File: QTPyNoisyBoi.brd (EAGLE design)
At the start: 30.5 x 128.5 mm, 32 parts, among them IC1 LD117AS50TR, IC2 TL074D, J1 WQP-PJ301M-12_JACK, J2 WQP-PJ301M-12_JACK, J3 WQP-PJ301M-12_JACK, J4 WQP-PJ301M-12_JACK, U1 ADAFRUIT_QTPYM0

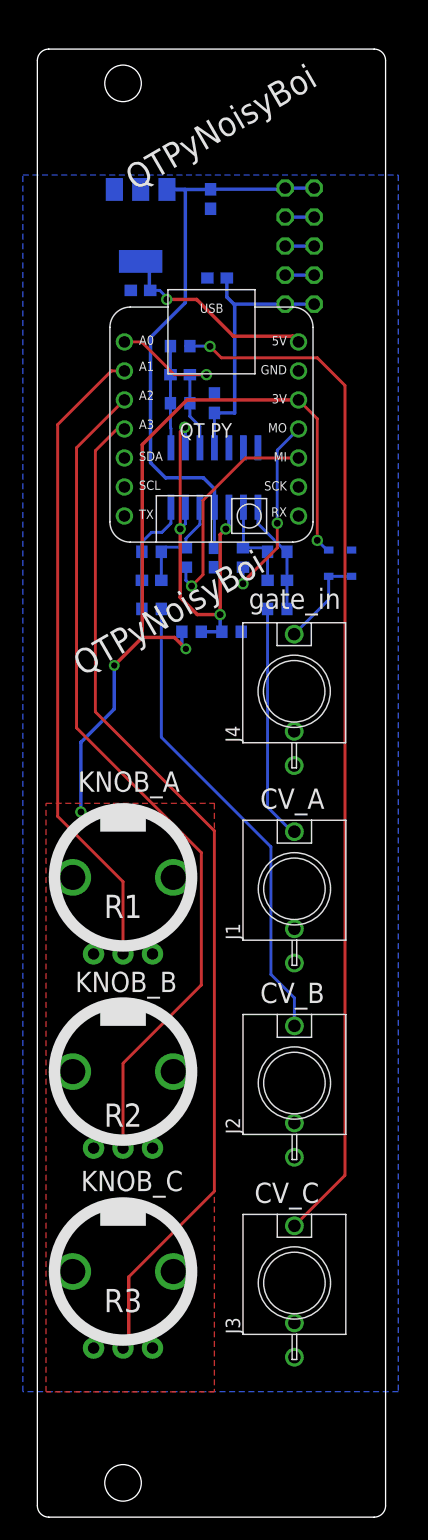
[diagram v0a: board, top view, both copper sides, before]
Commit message: added cap on vmidref; various cleanup
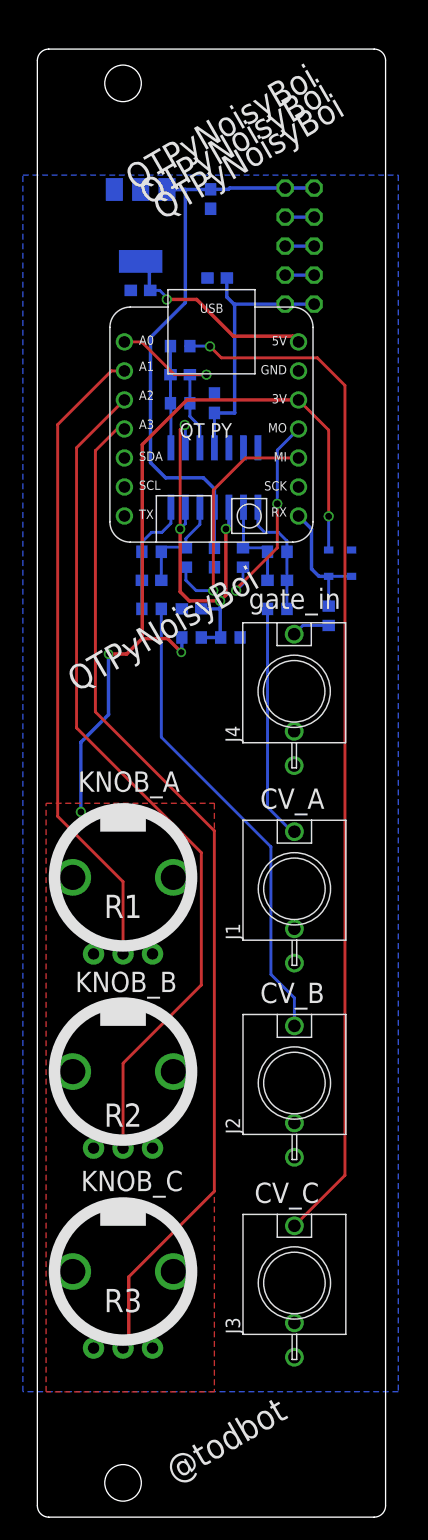
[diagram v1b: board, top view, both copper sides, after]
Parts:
- added C9: (no value), rcl:C0603
- added R14: (no value), rcl:R0603
- moved R11 0.51 mm to (16.9, 77.0)
- moved R10 0.50 mm to (13.5, 77.0)
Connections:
- new net N$5: J4.P$1, R14.2
- net GND: now also C9.1
- net RX: now also R14.1, U1.RX; no longer J4.P$1
- net VMIDREF: now also C9.2
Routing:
- net N$5: track 0.00 -> 3.34 mm
- net RX: track 8.31 -> 11.5 mm
- net N$6: track 17.0 -> 18.7 mm
- net N$7: track 19.7 -> 21.3 mm
- net VMIDREF: track 36.2 -> 37.8 mm
- net N$9: track 10.0 -> 10.7 mm
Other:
- board text added: "20210324"
- board text added: "@todbot"

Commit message: sigh
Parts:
- added C10: 18pF, rcl:C0603
- added C11: (no value), rcl:C0603
- added D3, D4: 250mA/100V, halcyonmod_DiscreteSemi:SOD-323
- added S1: MOMENTARY-SWITCH-SPST-PTH-6.0MM, SparkFun-Switches:TACTILE_SWITCH_PTH_6.0MM
- C4: value (none) -> 0.1uF
- R10, R11: value (none) -> 47k
- R4: value (none) -> 33k
- R5: value (none) -> 100k
- R6: value (none) -> 200
- moved R8 4.00 mm to (10.0, 80.5)
- moved R5 3.91 mm to (20.8, 80.6)
- moved J4 2.99 mm to (20.8, 69.8), turned to 270 degrees
- moved C2 2.55 mm to (16.0, 111.0), turned to 180 degrees
- moved C1 2.05 mm to (16.0, 113.5), turned to 0 degrees
- moved R9 1.30 mm to (10.0, 78.2), turned to 0 degrees
- moved R6 1.02 mm to (20.8, 78.5), turned to 180 degrees
- moved C4 0.73 mm to (20.8, 82.7)
- moved C5 0.60 mm to (10.0, 82.6)
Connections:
- net N$2 renamed A1
- net N$3 renamed A2
- net N$4 renamed A3
- net VMIDREF renamed VBIAS
- removed net N$15: J2.P$1, R9.2
- new net N$12: D4.C, DIM1.1, DIM1.2
- new net N$17: D3.A, DIM1.10, DIM1.9
- new net N$18: C10.2, IC2.1, R6.1
- new net N$2: S1.3, U1.TX
- new net N$8: IC2.13, IC2.14
- net +12V: now also D3.C; no longer DIM1.10, DIM1.9
- net -12V: now also D4.A; no longer DIM1.1, DIM1.2
- net GND: now also IC2.12, S1.1
- net N$1: now also J2.P$1, R9.2; no longer IC2.7, R9.1
- net N$10: now also C10.1
- net N$13: now also C11.1
- net N$14: now also C11.2, IC2.7, R9.1; no longer J1.P$1, R6.2
- net N$9: now also J1.P$1, R6.2; no longer IC2.1, R6.1
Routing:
- net N$15: track 41.3 -> 0.00 mm
- net N$1: track 10.5 -> 45.3 mm, vias 0 -> 1
- net N$18: track 0.00 -> 19.0 mm
- net N$2: track 0.00 -> 16.9 mm
- net A1: track 56.5 -> 72.7 mm
- net N$9: track 10.7 -> 26.4 mm, vias 0 -> 1
- net A3: track 89.5 -> 102.4 mm
- net A2: track 74.6 -> 86.6 mm
- net N$12: track 0.00 -> 7.84 mm
- net +12V: track 51.4 -> 43.9 mm
- net N$17: track 0.00 -> 7.15 mm
- net N$8: track 0.00 -> 5.59 mm
- net +3V3: track 70.1 -> 75.3 mm, vias 4 -> 3
- net N$5: track 3.34 -> 8.35 mm
- net N$10: track 8.36 -> 11.8 mm
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
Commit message: submit to fab
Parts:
- added C12: 18pF, rcl:C0603
- added R144: 220, rcl:R0603
- C1, C2: value (none) -> 1uF
- C11: value (none) -> 18pF
- C3, C5, C6, C7, C8, C9: value (none) -> 0.1uF
- R1, R2, R3: value (none) -> 10k
- R10, R11: value 47k -> 33k
- R12, R7: value (none) -> 33k
- R13, R8: value (none) -> 100k
- R14, R9: value (none) -> 200
- moved R14 28.1 mm to (12.5, 103.8), turned to 0 degrees
- moved R12 2.84 mm to (15.3, 98.0), turned to 270 degrees
- moved C7 2.16 mm to (17.6, 98.0)
- moved R13 0.80 mm to (12.5, 101.7), turned to 0 degrees
- moved C8 0.40 mm to (12.5, 99.6)
- moved C3 0.20 mm to (9.03, 107.6)
- moved R9 0.20 mm to (10.0, 78.4)
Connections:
- removed net N$16: J3.P$1, R13.2
- new net N$3: C12.2, IC2.8, R14.1
- new net N$4: C12.1, C8.1, IC2.10, R12.2, R13.1
- net A0: no longer C8.1, IC2.10
- net N$11: now also J3.P$1, R13.2, R14.2; no longer IC2.8, R12.2, R13.1
- net N$5: now also R144.2; no longer R14.2
- net RX: now also R144.1; no longer R14.1
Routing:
- net N$16: track 91.2 -> 0.00 mm, vias 1 -> 0
- net N$11: track 8.94 -> 98.1 mm, vias 0 -> 1
- net N$3: track 0.00 -> 18.1 mm
- net N$4: track 0.00 -> 10.6 mm
- net +12V: track 43.9 -> 53.6 mm
- net A0: track 16.6 -> 10.3 mm
- net -12V: track 20.7 -> 22.5 mm
- net A1: track 72.7 -> 72.0 mm
- net N$14: track 19.8 -> 19.1 mm
- net VBIAS: track 37.8 -> 37.2 mm
- net N$1: track 45.3 -> 45.9 mm
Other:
- board text added: "20210331"
- board text added: "github.com/todbot/QTPyNoisyBoi"
- board text added: "works w/ CircuitPython!"
- board text removed: "20210324"
- board text removed: "QTPyNoisyBoi"

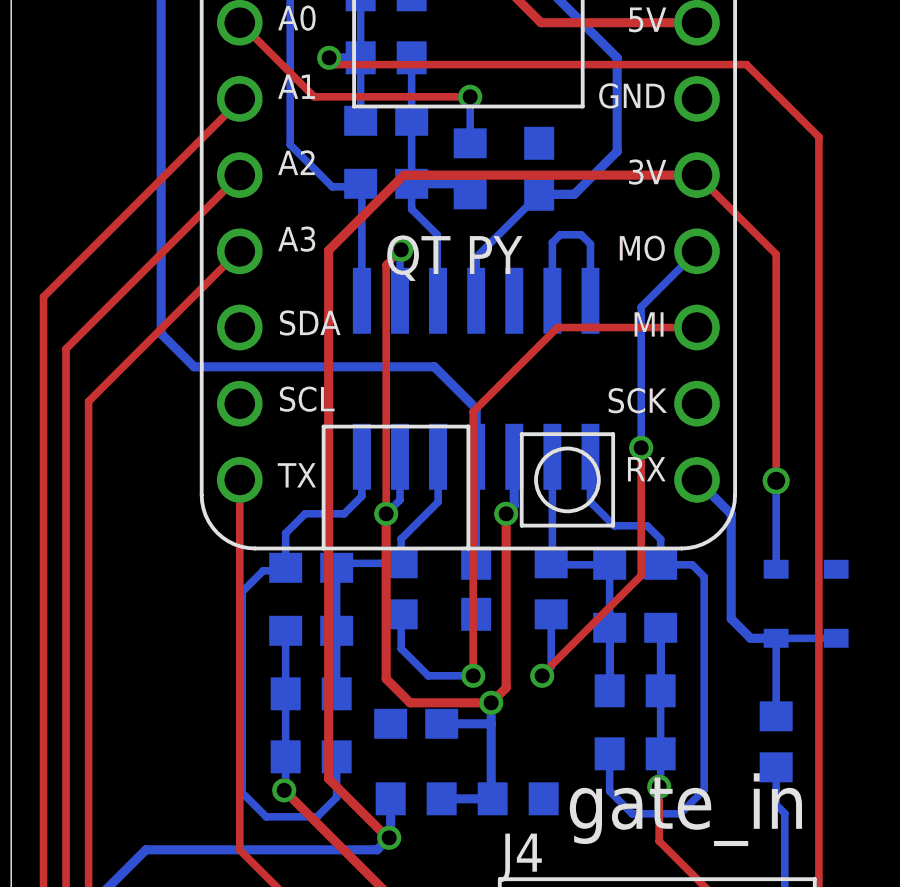
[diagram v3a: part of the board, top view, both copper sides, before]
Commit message: fix dumb +/- opamp input swap on B and C
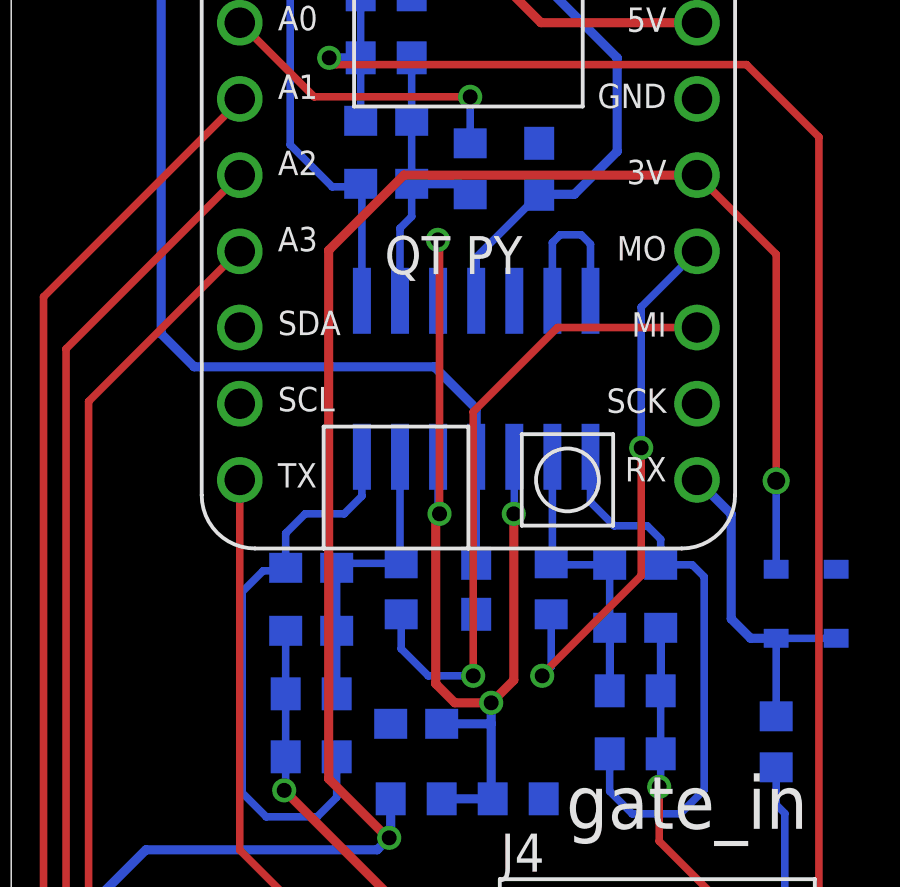
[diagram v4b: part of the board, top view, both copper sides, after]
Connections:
- net N$13: now also IC2.6; no longer IC2.5
- net N$4: now also IC2.9; no longer IC2.10
- net VBIAS: now also IC2.10, IC2.5; no longer IC2.6, IC2.9
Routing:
- net VBIAS: track 37.2 -> 36.0 mm
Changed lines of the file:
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@@
 <setting verticaltext="up"/>
 </settings>
-<grid distance="0.003333" unitdist="inch" unit="inch" style="lines" multiple="1" display="yes" altdistance="1" altunitdist="mm" altunit="mm"/>
+<grid distance="0.005" unitdist="inch" unit="inch" style="lines" multiple="1" display="no" altdistance="0.05" altunitdist="inch" altunit="inch"/>
 <layers>
-<layer number="1" name="Top" color="4" fill="1" visible="no" active="yes"/>
+<layer number="1" name="Top" color="4" fill="1" visible="yes" active="yes"/>
 <layer number="2" name="Route2" color="16" fill="1" visible="no" active="no"/>
 <layer number="3" name="Route3" color="17" fill="1" visible="no" active="no"/>
@@
 <layer number="20" name="Dimension" color="15" fill="1" visible="yes" active="yes"/>
 <layer number="21" name="tPlace" color="7" fill="1" visible="no" active="yes"/>
-<layer number="22" name="bPlace" color="7" fill="1" visible="yes" active="yes"/>
+<layer number="22" name="bPlace" color="7" fill="1" visible="no" active="yes"/>
 <layer number="23" name="tOrigins" color="15" fill="1" visible="no" active="yes"/>
-<layer number="24" name="bOrigins" color="15" fill="1" visible="yes" active="yes"/>
+<layer number="24" name="bOrigins" color="15" fill="1" visible="no" active="yes"/>
 <layer number="25" name="tNames" color="7" fill="1" visible="no" active="yes"/>
-<layer number="26" name="bNames" color="7" fill="1" visible="yes" active="yes"/>
+<layer number="26" name="bNames" color="7" fill="1" visible="no" active="yes"/>
 <layer number="27" name="tValues" color="7" fill="1" visible="no" active="yes"/>
 <layer number="28" name="bValues" color="7" fill="1" visible="no" active="yes"/>
@@
 <layer number="37" name="tTest" color="7" fill="1" visible="no" active="yes"/>
 <layer number="38" name="bTest" color="7" fill="1" visible="no" active="yes"/>
-<layer number="39" name="tKeepout" color="4" fill="11" visible="no" active="yes"/>
+<layer number="39" name="tKeepout" color="4" fill="11" visible="yes" active="yes"/>
 <layer number="40" name="bKeepout" color="1" fill="11" visible="yes" active="yes"/>
-<layer number="41" name="tRestrict" color="4" fill="10" visible="no" active="yes"/>
+<layer number="41" name="tRestrict" color="4" fill="10" visible="yes" active="yes"/>
 <layer number="42" name="bRestrict" color="1" fill="10" visible="yes" active="yes"/>
 <layer number="43" name="vRestrict" color="2" fill="10" visible="no" active="yes"/>
@@
 <layer number="45" name="Holes" color="7" fill="1" visible="yes" active="yes"/>
 <layer number="46" name="Milling" color="3" fill="1" visible="no" active="yes"/>
-<layer number="47" name="Measures" color="7" fill="1" visible="yes" active="yes"/>
-<layer number="48" name="Document" color="7" fill="1" visible="yes" active="yes"/>
-<layer number="49" name="Reference" color="7" fill="1" visible="yes" active="yes"/>
+<layer number="47" name="Measures" color="7" fill="1" visible="no" active="yes"/>
+<layer number="48" name="Document" color="7" fill="1" visible="no" active="yes"/>
+<layer number="49" name="Reference" color="7" fill="1" visible="no" active="yes"/>
 <layer number="50" name="dxf" color="7" fill="1" visible="no" active="no"/>
 <layer number="51" name="tDocu" color="7" fill="1" visible="no" active="yes"/>
-<layer number="52" name="bDocu" color="7" fill="1" visible="yes" active="yes"/>
+<layer number="52" name="bDocu" color="7" fill="1" visible="no" active="yes"/>
 <layer number="53" name="tGND_GNDA" color="7" fill="9" visible="no" active="no"/>
 <layer number="54" name="bGND_GNDA" color="1" fill="9" visible="no" active="no"/>
@@
 <contactref element="C5" pad="1"/>
 <contactref element="R7" pad="2"/>
-<contactref element="IC2" pad="5"/>
 <wire x1="10.85" y1="82.6" x2="10.85" y2="80.5" width="0.254" layer="16"/>
-<wire x1="13" y1="84.85" x2="13" y2="85.662" width="0.254" layer="16"/>
-<wire x1="14.23" y1="86.892" x2="13" y2="85.662" width="0.254" layer="16"/>
-<wire x1="14.23" y1="88.4" x2="14.23" y2="86.892" width="0.254" layer="16"/>
 <contactref element="C11" pad="1"/>
 <wire x1="13" y1="84.85" x2="11" y2="84.85" width="0.254" layer="16"/>
 <wire x1="11" y1="84.85" x2="10.85" y2="84.7" width="0.254" layer="16"/>
 <wire x1="10.85" y1="84.7" x2="10.85" y2="82.6" width="0.254" layer="16"/>
+<contactref element="IC2" pad="6"/>
+<wire x1="12.96" y1="88.4" x2="12.96" y2="84.89" width="0.254" layer="16"/>
+<wire x1="12.96" y1="84.89" x2="13" y2="84.85" width="0.254" layer="16"/>
 </signal>
 <signal name="+12V">
@@
 <contactref element="R11" pad="2"/>
 <contactref element="IC2" pad="3"/>
-<contactref element="IC2" pad="6"/>
 <wire x1="16.05" y1="77" x2="14.35" y2="77" width="0.3048" layer="16"/>
 <wire x1="16.05" y1="77" x2="16" y2="77.05" width="0.3048" layer="16"/>
@@
 <via x="16" y="80.2" extent="1-16" drill="0.5"/>
 <wire x1="16" y1="79.5" x2="16" y2="80.2" width="0.3048" layer="16"/>
-<wire x1="16" y1="80.2" x2="16.5" y2="80.7" width="0.3048" layer="1"/>
-<wire x1="16.5" y1="86.5" x2="16.5" y2="80.7" width="0.3048" layer="1"/>
-<via x="16.5" y="86.5" extent="1-16" drill="0.5"/>
-<wire x1="16.5" y1="86.5" x2="16.77" y2="86.77" width="0.3048" layer="16"/>
-<wire x1="16.77" y1="86.77" x2="16.77" y2="88.4" width="0.3048" layer="16"/>
-<wire x1="12.96" y1="88.4" x2="12.96" y2="86.96" width="0.254" layer="16"/>
-<wire x1="12.96" y1="86.96" x2="12.5" y2="86.5" width="0.254" layer="16"/>
-<via x="12.5" y="86.5" extent="1-16" drill="0.5"/>
-<wire x1="12.5" y1="86.5" x2="12.5" y2="81" width="0.3048" layer="1"/>
-<wire x1="12.5" y1="81" x2="13.3" y2="80.2" width="0.3048" layer="1"/>
-<wire x1="16" y1="80.2" x2="13.3" y2="80.2" width="0.3048" layer="1"/>
-<contactref element="IC2" pad="9"/>
-<wire x1="12.96" y1="93.6" x2="12.96" y2="95.26" width="0.254" layer="16"/>
-<wire x1="12.96" y1="95.26" x2="13" y2="95.3" width="0.254" layer="16"/>
-<via x="13" y="95.3" extent="1-16" drill="0.5"/>
-<wire x1="12.5" y1="86.5" x2="12.5" y2="94.8" width="0.254" layer="1"/>
-<wire x1="12.5" y1="94.8" x2="13" y2="95.3" width="0.254" layer="1"/>
+<wire x1="16" y1="80.2" x2="16.754" y2="80.954" width="0.3048" layer="1"/>
+<wire x1="16.754" y1="86.5" x2="16.754" y2="80.954" width="0.3048" layer="1"/>
+<via x="16.754" y="86.5" extent="1-16" drill="0.5"/>
+<via x="14.278" y="86.5" extent="1-16" drill="0.5"/>
+<wire x1="14.278" y1="86.5" x2="14.151" y2="86.373" width="0.3048" layer="1"/>
+<wire x1="14.151" y1="86.373" x2="14.151" y2="80.835" width="0.3048" layer="1"/>
+<wire x1="16" y1="80.2" x2="14.786" y2="80.2" width="0.3048" layer="1"/>
+<wire x1="14.786" y1="80.2" x2="14.151" y2="80.835" width="0.3048" layer="1"/>
 <contactref element="C9" pad="2"/>
 <wire x1="14.35" y1="79.5" x2="16" y2="79.5" width="0.3048" layer="16"/>
+<contactref element="IC2" pad="5"/>
+<contactref element="IC2" pad="10"/>
+<wire x1="14.278" y1="95.577" x2="14.224" y2="95.631" width="0.254" layer="1"/>
+<via x="14.224" y="95.631" extent="1-16" drill="0.5"/>
+<wire x1="14.224" y1="95.631" x2="14.224" y2="93.606" width="0.254" layer="16"/>
+<wire x1="14.224" y1="93.606" x2="14.23" y2="93.6" width="0.254" layer="16"/>
+<wire x1="14.278" y1="86.5" x2="14.278" y2="95.577" width="0.254" layer="1"/>
+<wire x1="14.23" y1="88.4" x2="14.23" y2="86.548" width="0.254" layer="16"/>
+<wire x1="14.23" y1="86.548" x2="14.278" y2="86.5" width="0.254" layer="16"/>
+<wire x1="16.77" y1="88.4" x2="16.77" y2="86.516" width="0.254" layer="16"/>
+<wire x1="16.77" y1="86.516" x2="16.754" y2="86.5" width="0.254" layer="16"/>
 </signal>
 <signal name="N$11">
@@
 </signal>
 <signal name="N$4">
-<contactref element="IC2" pad="10"/>
 <contactref element="R12" pad="2"/>
 <contactref element="C12" pad="1"/>
 <contactref element="R13" pad="1"/>
 <contactref element="C8" pad="1"/>
-<wire x1="14.23" y1="93.6" x2="14.2" y2="93.63" width="0.254" layer="16"/>
-<wire x1="14.2" y1="93.63" x2="14.2" y2="95.8" width="0.254" layer="16"/>
-<wire x1="14.2" y1="95.8" x2="13.35" y2="96.65" width="0.254" layer="16"/>
-<wire x1="13.35" y1="96.65" x2="13.35" y2="97.5" width="0.254" layer="16"/>
 <wire x1="13.35" y1="97.5" x2="13.35" y2="99.6" width="0.254" layer="16"/>
 <wire x1="13.35" y1="101.7" x2="13.35" y2="99.6" width="0.254" layer="16"/>
 <wire x1="13.35" y1="97.5" x2="14.95" y2="97.5" width="0.3048" layer="16"/>
 <wire x1="14.95" y1="97.5" x2="15.3" y2="97.15" width="0.3048" layer="16"/>
+<contactref element="IC2" pad="9"/>
+<wire x1="13.35" y1="97.5" x2="13.35" y2="96.408" width="0.254" layer="16"/>
+<wire x1="12.96" y1="96.018" x2="12.96" y2="93.6" width="0.254" layer="16"/>
+<wire x1="13.35" y1="96.408" x2="12.96" y2="96.018" width="0.254" layer="16"/>
 </signal>
 </signals>
